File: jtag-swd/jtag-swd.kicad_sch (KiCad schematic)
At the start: 7 parts, among them J1 Conn_02x10_Odd_Even, J2 Conn_02x10_Odd_Even, J3 uart_host_2.54, SW1 Reset

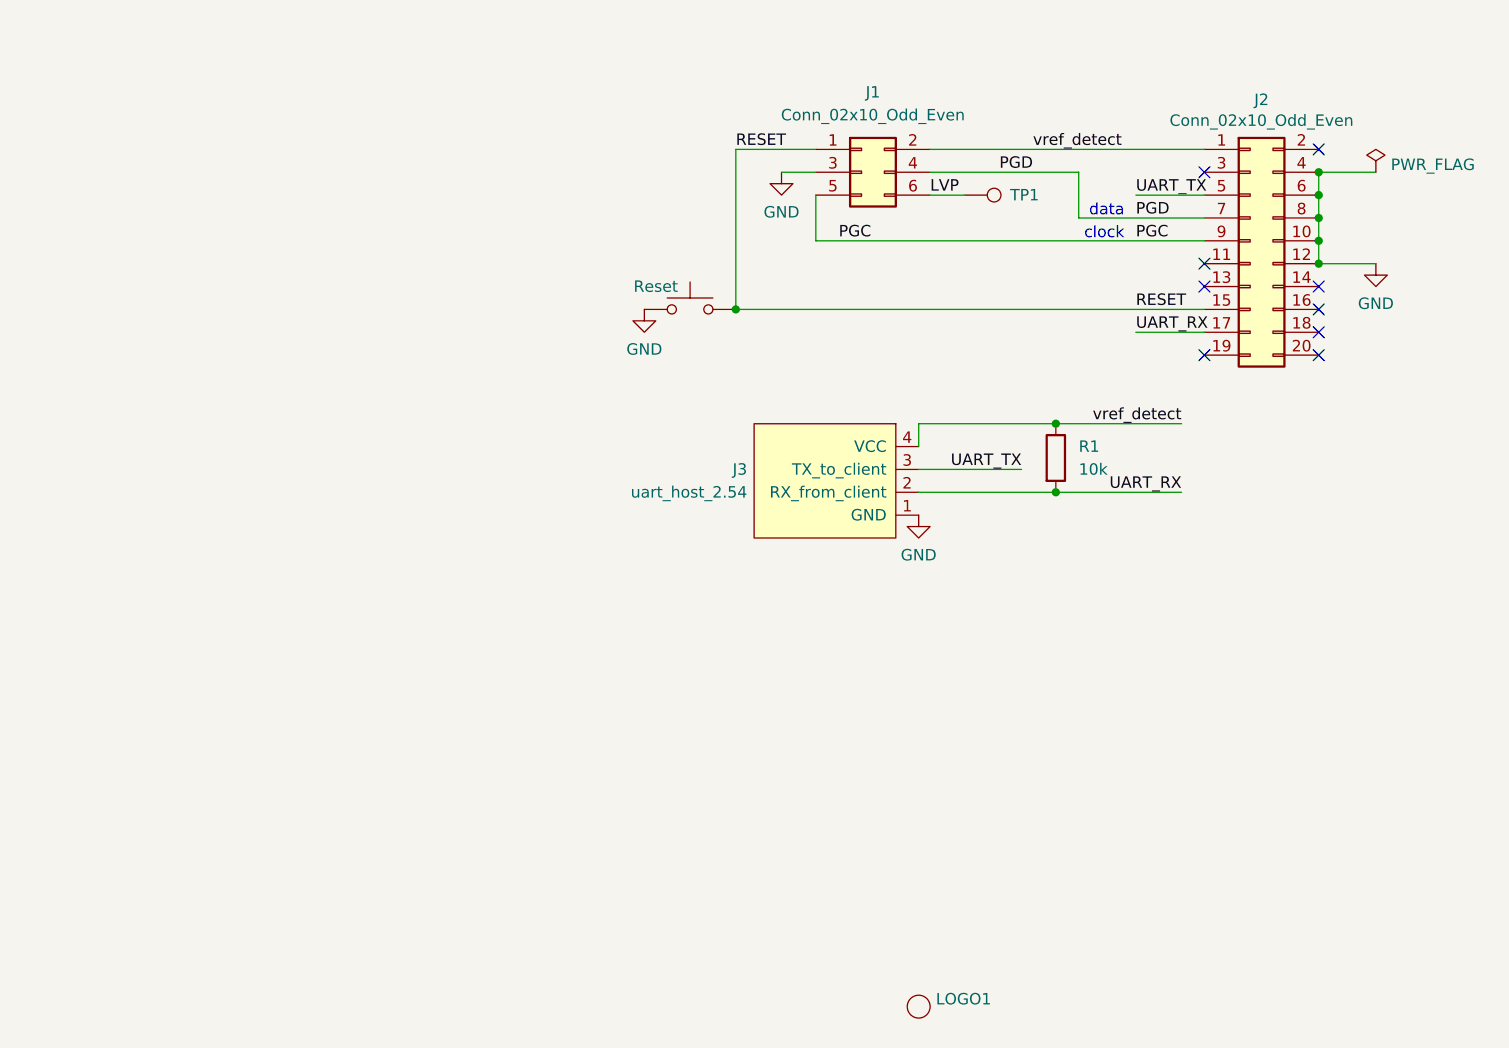
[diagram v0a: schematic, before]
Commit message: Modernize the adapter boards
This repo contains adapter boards for the Jitter 6-pins REDFit debug
interface to multiple standard programming/debug tools.
Each now renamed to make this clearer (BMP/HSProbe/JLink) and save those
projects as modern Kicad10 designs
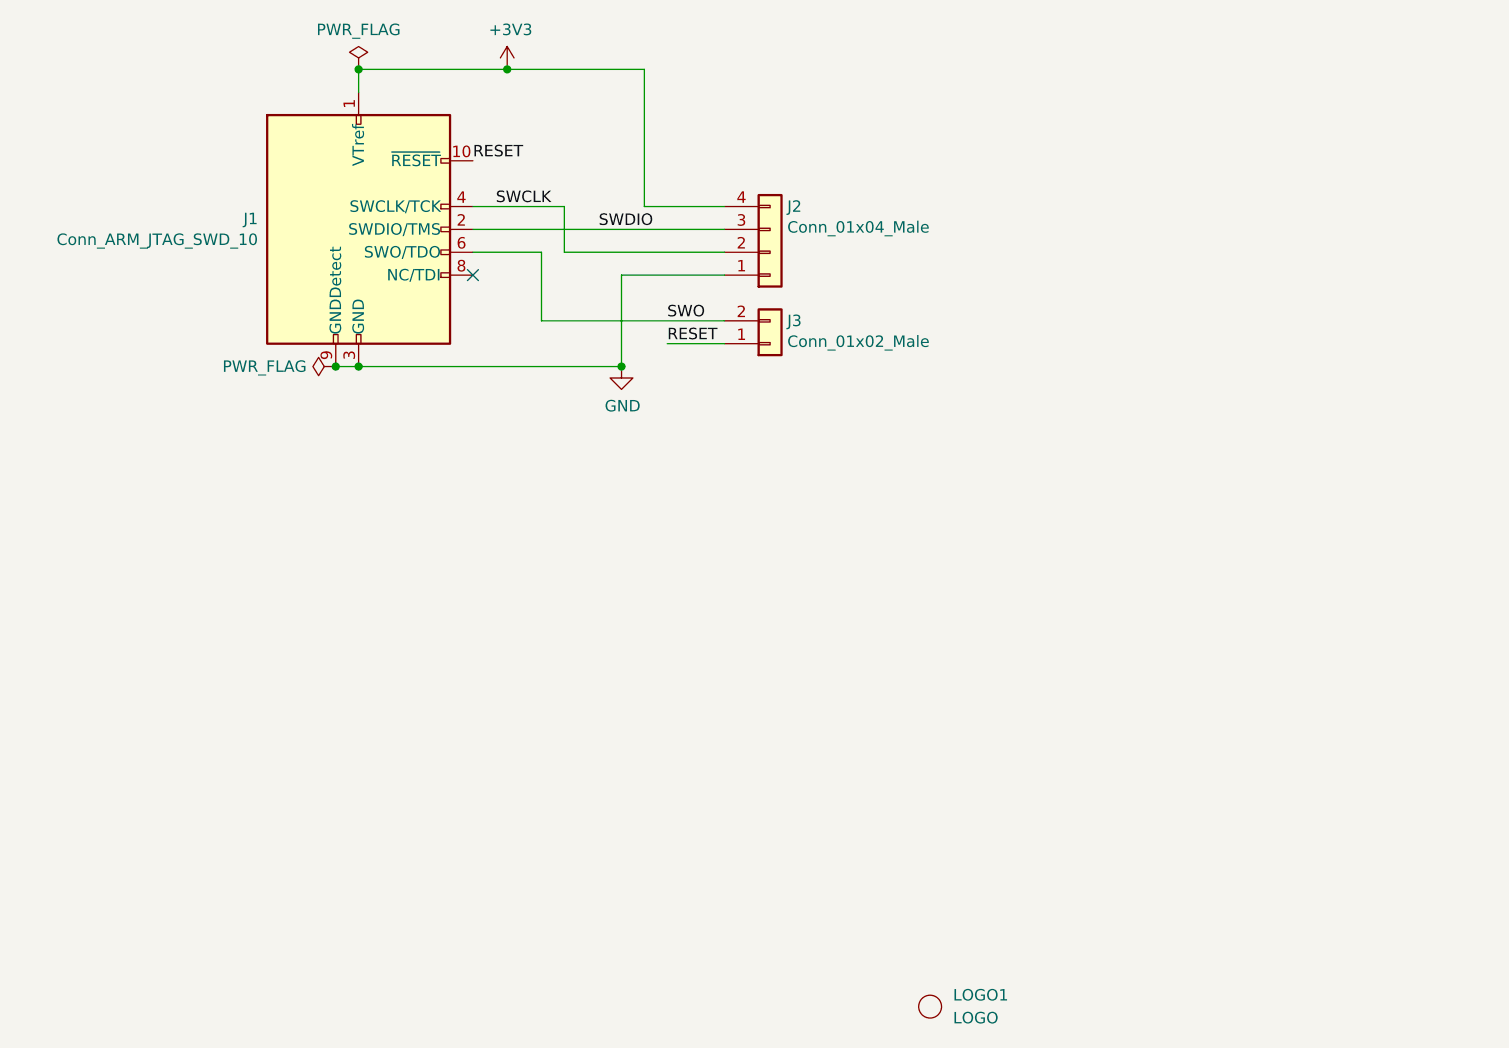
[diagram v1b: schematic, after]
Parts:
- removed J1: Conn_02x10_Odd_Even, Connector_IDC:IDC-Header_2x03_P2.54mm_Vertical, symbol Connector_Generic:Conn_02x03_Odd_Even
- removed J2: Conn_02x10_Odd_Even, Jitter_Connectors:JLink_PinHeader_2x10_2.54_Horizontal, symbol Connector_Generic:Conn_02x10_Odd_Even
- removed J3: uart_host_2.54, Connector_PinHeader_2.54mm:PinHeader_1x04_P2.54mm_Vertical, symbol Jitter_Components:uart_host_2.54
- removed R1: 10k, Resistor_SMD:R_0603_1608Metric, symbol Device:R
- removed SW1: Reset, Button_Switch_SMD:SW_SPST_EVQPE1, symbol Switch:SW_Push
- removed TP1: TestPoint, TestPoint:TestPoint_THTPad_D1.0mm_Drill0.5mm, symbol Connector:TestPoint
- added J1: Conn_ARM_JTAG_SWD_10, Jitter_Footprints:PinSocket_2x05_P1.27mm_Vertical_Mirrored_Y, symbol Connector:Conn_ARM_JTAG_SWD_10
- added J2: Conn_01x04_Male, Connector_PinHeader_2.54mm:PinHeader_1x04_P2.54mm_Horizontal, symbol Connector_Generic:Conn_01x04
- added J3: Conn_01x02_Male, Connector_PinHeader_2.54mm:PinHeader_1x02_P2.54mm_Vertical, symbol Connector_Generic:Conn_01x02
- LOGO1: footprint Jitter_Logos:JitterLogo -> Jitter_Logos:Jitter-micro
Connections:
- net GND: now also J1.3 (GND), J1.5 (GND), J1.9 (GNDDetect), J2.1 (Pin_1)
- net RESET: now also J1.10 (~{RESET}), J3.1 (Pin_1)
- new net +3V3: J1.1 (VTref), J2.4 (Pin_4)
- new net SWCLK: J1.4 (SWCLK/TCK), J2.2 (Pin_2)
- new net SWDIO: J1.2 (SWDIO/TMS), J2.3 (Pin_3)
- new net SWO: J1.6 (SWO/TDO), J3.2 (Pin_2)
- no-connect marks 9 -> 1
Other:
- note removed: "clock"
- note removed: "data"
- company: Jitter -> (none)
- title: Jlink to TC2030-IDC__microchip adapter -> JTAG-SWD
